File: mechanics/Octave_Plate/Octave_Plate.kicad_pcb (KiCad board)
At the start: 2 copper layers, 81.2 x 62.2 mm, 0 parts

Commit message: Update plate design
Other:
- board size 81.2 x 62.2 mm -> 81.3 x 62.2 mm
- board text added: "Octave Plate 1.0.1"
- board text removed: "Octave Plate 1.0.0"

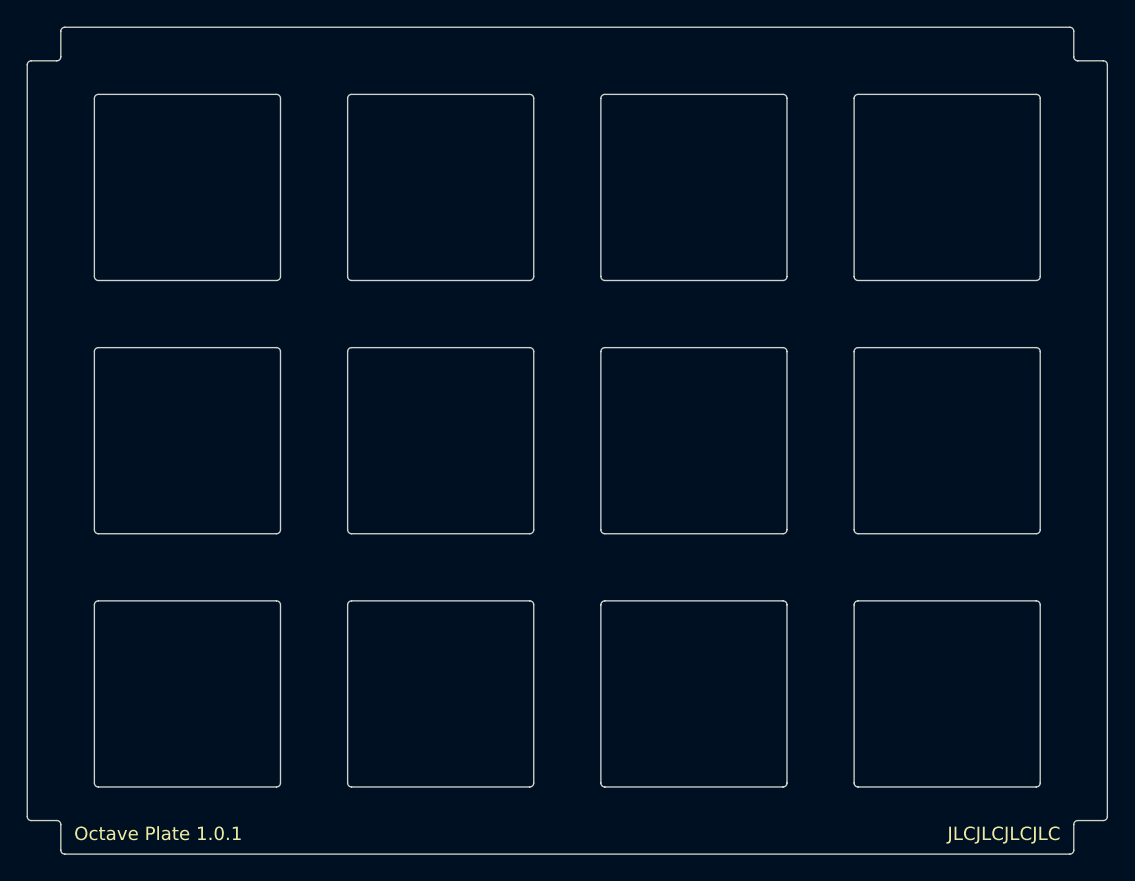
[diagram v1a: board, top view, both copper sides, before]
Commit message: Change plate design
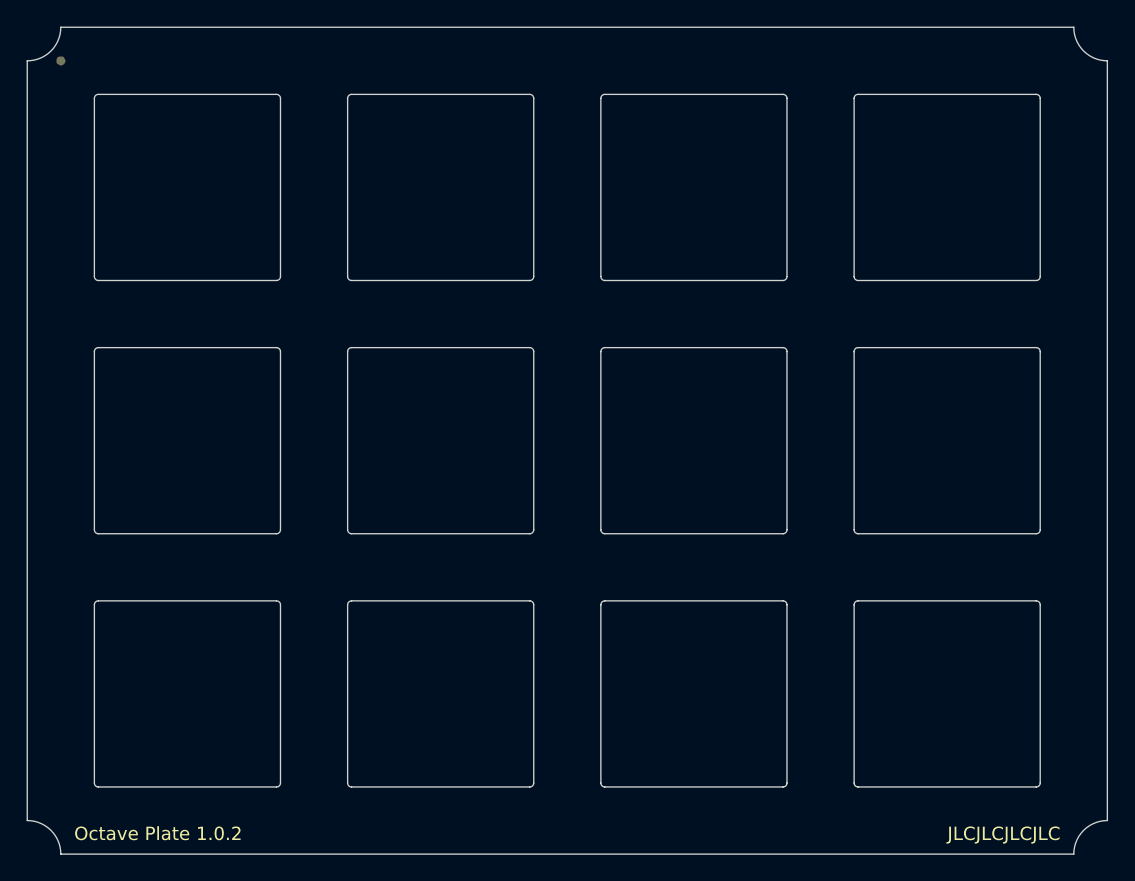
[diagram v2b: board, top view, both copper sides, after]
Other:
- board size 81.3 x 62.2 mm -> 81.2 x 62.2 mm
- board text added: "Octave Plate 1.0.2"
- board text removed: "Octave Plate 1.0.1"

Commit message: Modify PCB and plate
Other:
- outline, holes or cut-outs redrawn
- board text added: "Octave Plate 1.0.3"
- board text removed: "Octave Plate 1.0.2"
